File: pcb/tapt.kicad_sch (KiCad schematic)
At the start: 22 parts, among them SW1 SW_SPDT_XKB_DMx-xxxx-1, U1 nRF52810-QCxx, Y1 32MHz

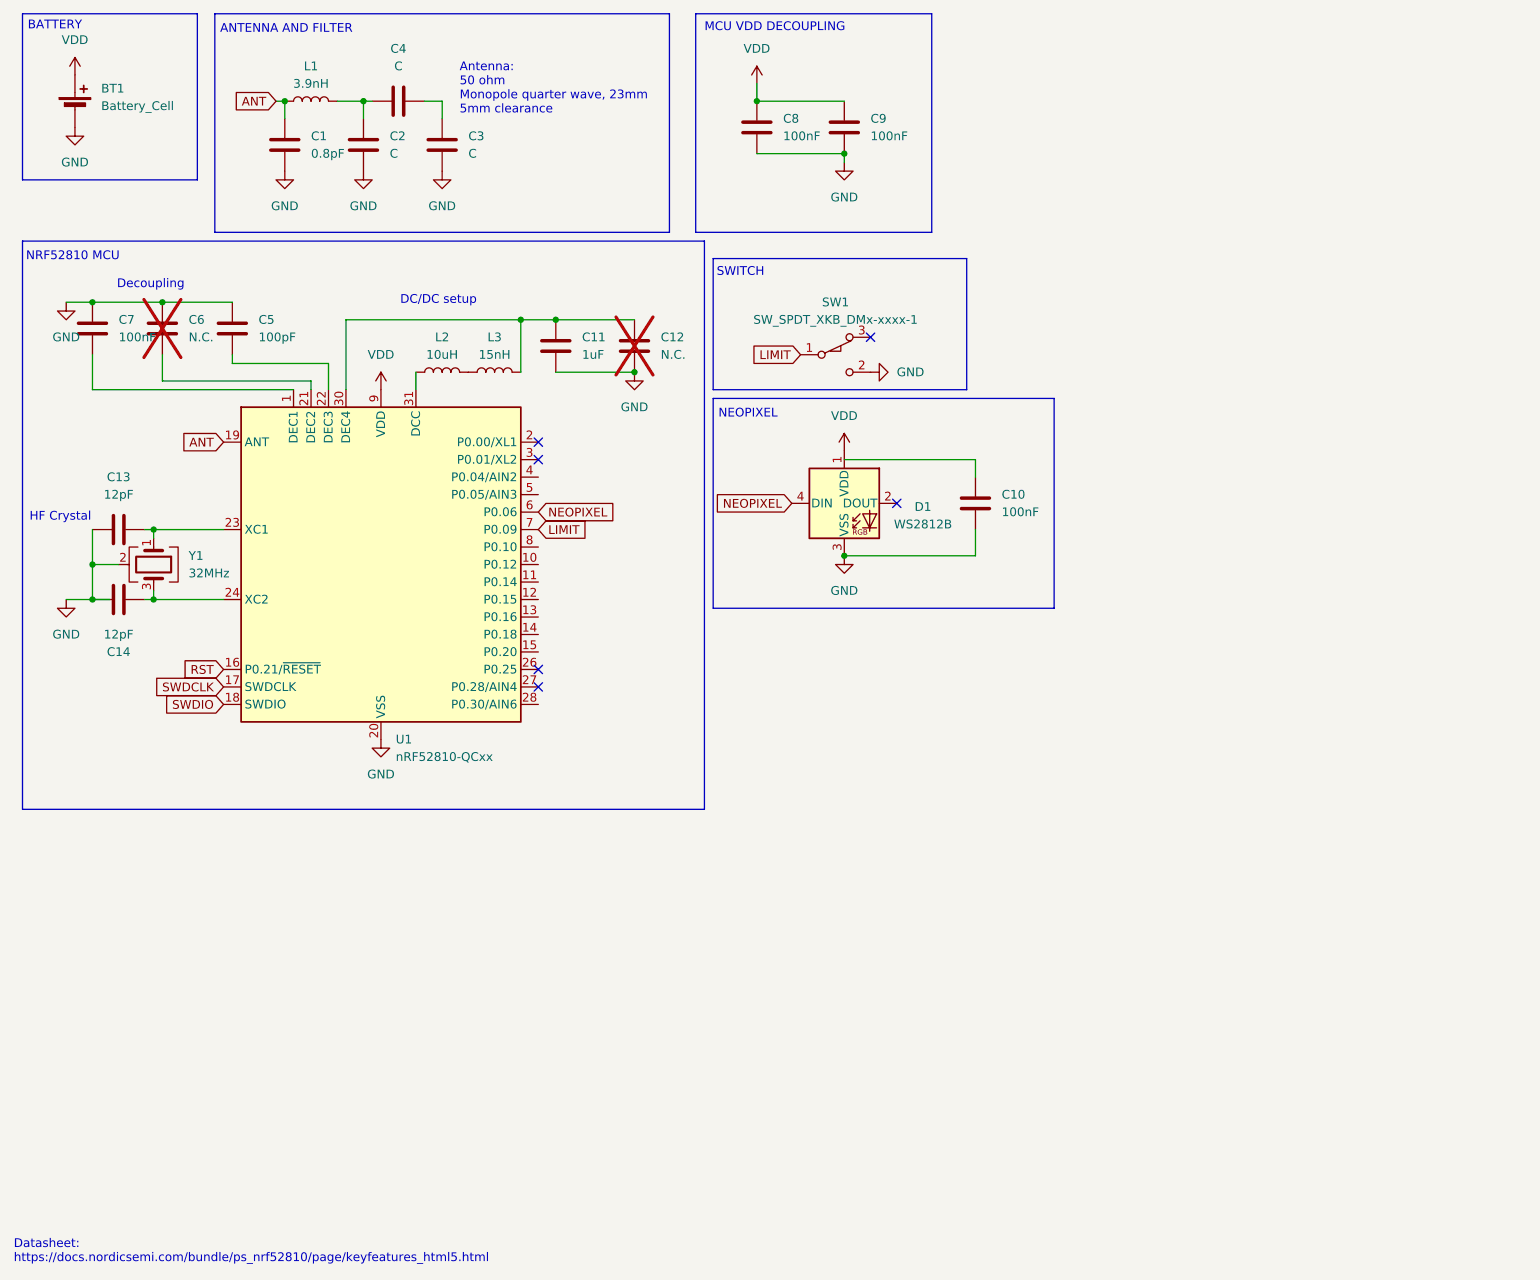
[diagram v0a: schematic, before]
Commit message: schematic: antenna, reset button
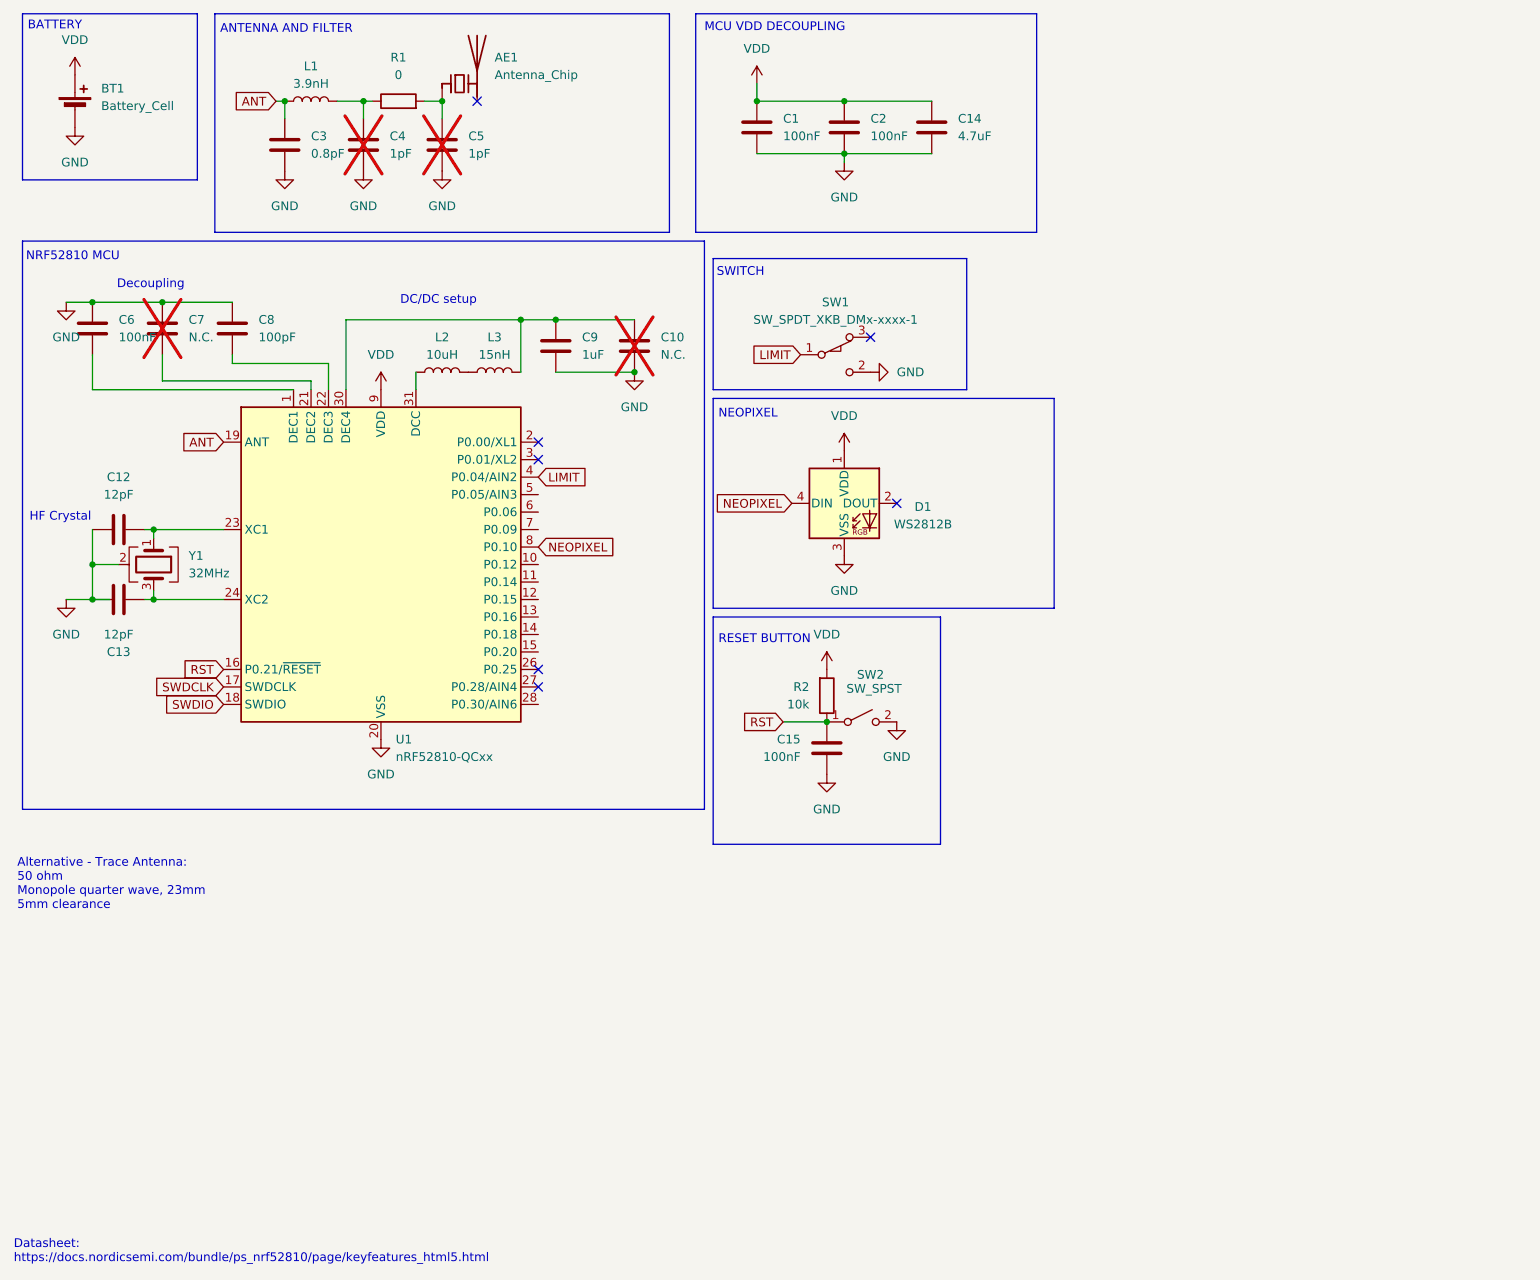
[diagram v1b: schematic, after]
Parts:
- removed C10: 100nF, Capacitor_SMD:C_0402_1005Metric, symbol Device:C
- removed C3, C4: C, symbol Device:C
- added AE1: Antenna_Chip, Inductor_SMD:L_1206_3216Metric, symbol Device:Antenna_Chip
- added C14: 4.7uF, Capacitor_SMD:C_0603_1608Metric, symbol Device:C
- added C15: 100nF, Capacitor_SMD:C_0402_1005Metric, symbol Device:C
- added C5: 1pF, Capacitor_SMD:C_0402_1005Metric, symbol Device:C
- added R1: 0, Resistor_SMD:R_0402_1005Metric, symbol Device:R
- added R2: 10k, Resistor_SMD:R_0402_1005Metric, symbol Device:R
- added SW2: SW_SPST, Button_Switch_SMD:SW_SPST_TS-1088-xR020, symbol Switch:SW_SPST
- C4: renamed from C2; value C -> 1pF; footprint (none) -> Capacitor_SMD:C_0402_1005Metric; now not fitted
- L3: footprint (none) -> Inductor_SMD:L_0402_1005Metric; LCSC (none) -> C27143
- renumbered C8 to C1, C12 to C10, C13 to C12, C14 to C13, C9 to C2, C1 to C3, C7 to C6, C6 to C7, C5 to C8, C11 to C9
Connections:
- net GND: now also C14.2, C15.2, C5.2, SW2.2 (B)
- net LIMIT: now also U1.4 (P0.04/AIN2); no longer U1.7 (P0.09)
- net NEOPIXEL: now also U1.8 (P0.10); no longer U1.6 (P0.06)
- net RST: now also C15.1, R2.1, SW2.1 (A)
- net VDD: now also C14.1, R2.2
- net at C4.1, L1.2: now also R1.1
- new net: AE1.1 (FEED), C5.1, R1.2
- no-connect marks 6 -> 7
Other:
- note added: "Alternative - Trace Antenna: 50 ohm Monopole quarter wave, 23mm 5mm clearance"
- note added: "RESET BUTTON"
- note removed: "Antenna: 50 ohm Monopole quarter wave, 23mm 5mm clearance"

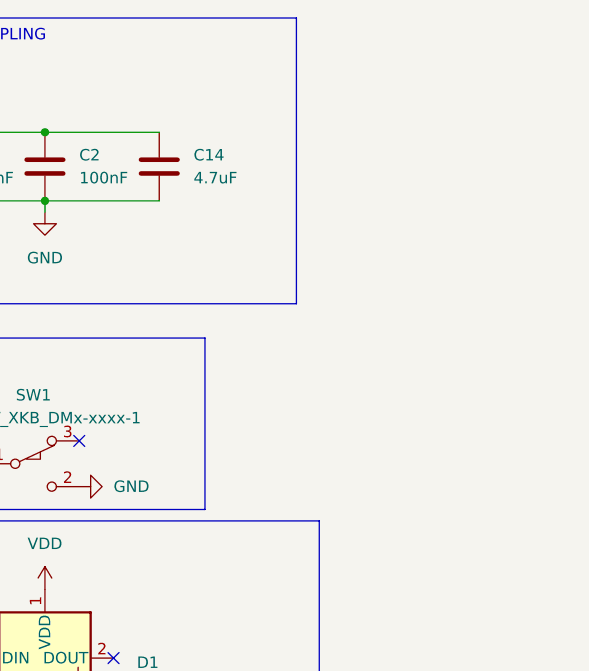
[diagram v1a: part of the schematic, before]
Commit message: major rf improvements, battery connector, component relayout
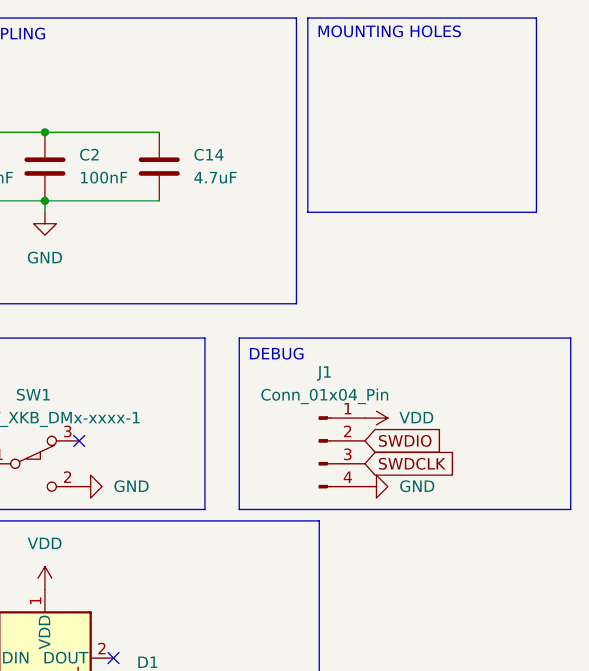
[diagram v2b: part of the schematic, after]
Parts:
- added J1: Conn_01x04_Pin, Connector_PinHeader_2.54mm:PinHeader_1x04_P2.54mm_Vertical, symbol Connector:Conn_01x04_Pin
- BT1: footprint Battery:BatteryHolder_MYOUNG_BS-07-A1BJ001_CR2032 -> Connector_Wire:SolderWire-0.5sqmm_1x02_P4.6mm_D0.9mm_OD2.1mm
- L2: footprint Capacitor_SMD:C_0603_1608Metric -> Inductor_SMD:L_0603_1608Metric
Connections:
- net GND: now also J1.4 (Pin_4)
- net SWDCLK: now also J1.3 (Pin_3)
- net SWDIO: now also J1.2 (Pin_2)
- net VDD: now also J1.1 (Pin_1)
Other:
- note added: "DEBUG"
- note added: "MOUNTING HOLES"
- company: (none) -> Siddhant Kameswar: @grimsteel
- title: (none) -> tapt

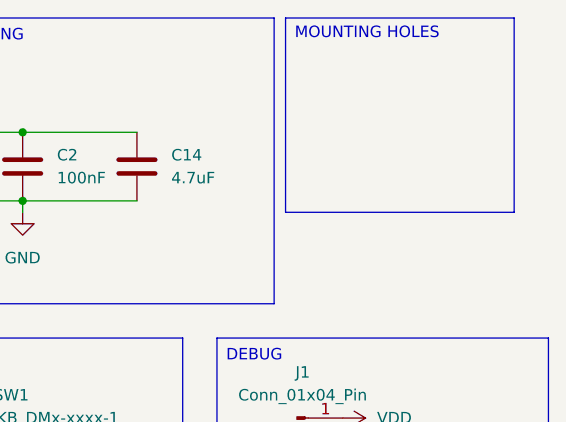
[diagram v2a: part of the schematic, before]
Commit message: add mounting holes on dogboned corners
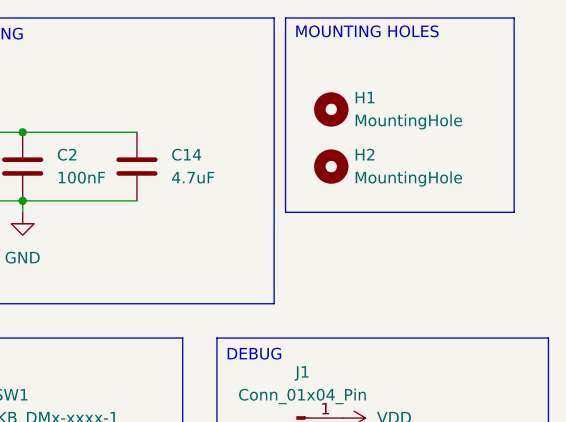
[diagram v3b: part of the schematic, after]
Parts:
- added H1, H2: MountingHole, MountingHole:MountingHole_2.7mm_M2.5, symbol Mechanical:MountingHole
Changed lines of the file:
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@@
+	)
+	(symbol
+		(lib_id "Mechanical:MountingHole")
+		(at 168.91 24.13 0)
+		(unit 1)
+		(exclude_from_sim no)
+		(in_bom no)
+		(on_board yes)
+		(dnp no)
+		(fields_autoplaced yes)
+		(property "Reference" "H1"
+			(at 171.45 22.8599 0)
+			(effects
+				(font
+					(size 1.27 1.27)
+				)
+				(justify left)
+			)
+		)
+		(property "Value" "MountingHole"
+			(at 171.45 25.3999 0)
+			(effects
+				(font
+					(size 1.27 1.27)
+				)
+				(justify left)
+			)
+		)
+		(property "Footprint" "MountingHole:MountingHole_2.7mm_M2.5"
+			(at 168.91 24.13 0)
+			(effects
+				(font
+					(size 1.27 1.27)
+				)
+				(hide yes)
+			)
+		)
+		(property "Datasheet" "~"
+			(at 168.91 24.13 0)
+			(effects
+				(font
+					(size 1.27 1.27)
+				)
+				(hide yes)
+			)
+		)
+		(property "Description" "Mounting Hole without connection"
+			(at 168.91 24.13 0)
+			(effects
+				(font
+					(size 1.27 1.27)
+				)
+				(hide yes)
+			)
+		)
+		(instances
+			(project ""
+				(path "/5229fa67-90ff-468b-81bc-87113a360bb5"
+					(reference "H1")
+					(unit 1)
+				)
+			)
+		)
 	)
 	(symbol
@@
 					(unit 1)
 				)
+			)
+		)
+	)
+	(symbol
+		(lib_id "Mechanical:MountingHole")
+		(at 168.91 30.48 0)
+		(unit 1)
+		(exclude_from_sim no)
+		(in_bom no)
+		(on_board yes)
+		(dnp no)
+		(fields_autoplaced yes)
+		(property "Reference" "H2"
+			(at 171.45 29.2099 0)
+			(effects
+				(font
+					(size 1.27 1.27)
+				)
+				(justify left)
+			)
+		)
+		(property "Value" "MountingHole"
+			(at 171.45 31.7499 0)
+			(effects
+				(font
+					(size 1.27 1.27)
+				)
+				(justify left)
+			)
+		)
+		(property "Footprint" "MountingHole:MountingHole_2.7mm_M2.5"
+			(at 168.91 30.48 0)
+			(effects
+				(font
+					(size 1.27 1.27)
+				)
+				(hide yes)
+			)
+		)
+		(property "Datasheet" "~"
+			(at 168.91 30.48 0)
+			(effects
+				(font
+					(size 1.27 1.27)
+				)
+				(hide yes)
+			)
+		)
+		(property "Description" "Mounting Hole without connection"
+			(at 168.91 30.48 0)
+			(effects
+				(font
+					(size 1.27 1.27)
+				)
+				(hide yes)
+			)
+		)
+		(instances
+			(project "tapt"
+				(path "/5229fa67-90ff-468b-81bc-87113a360bb5"
+					(reference "H2")
+					(unit 1)
+				)

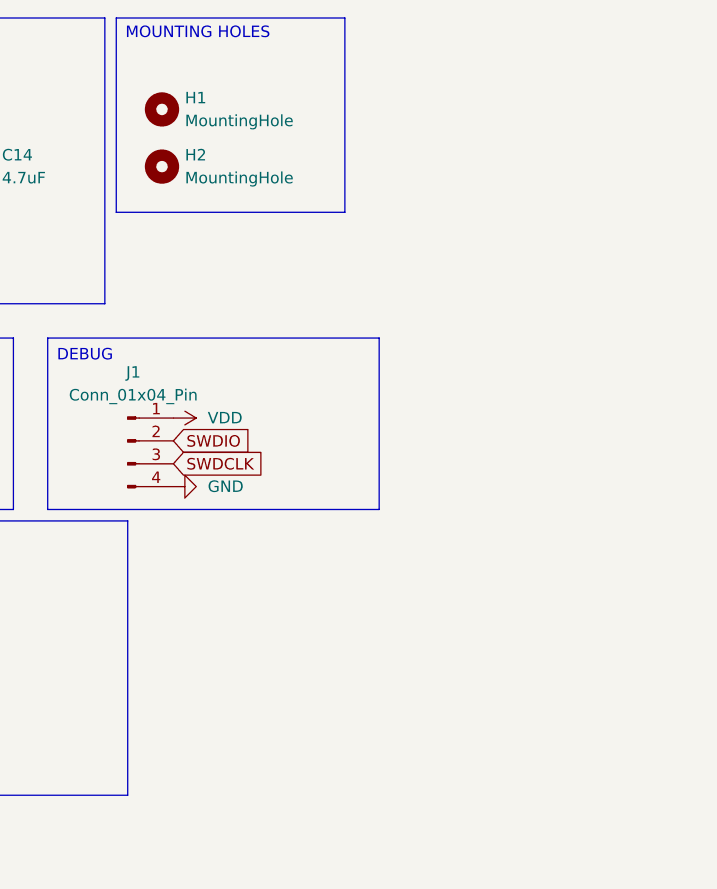
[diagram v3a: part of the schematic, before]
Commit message: schematic: status led, uart
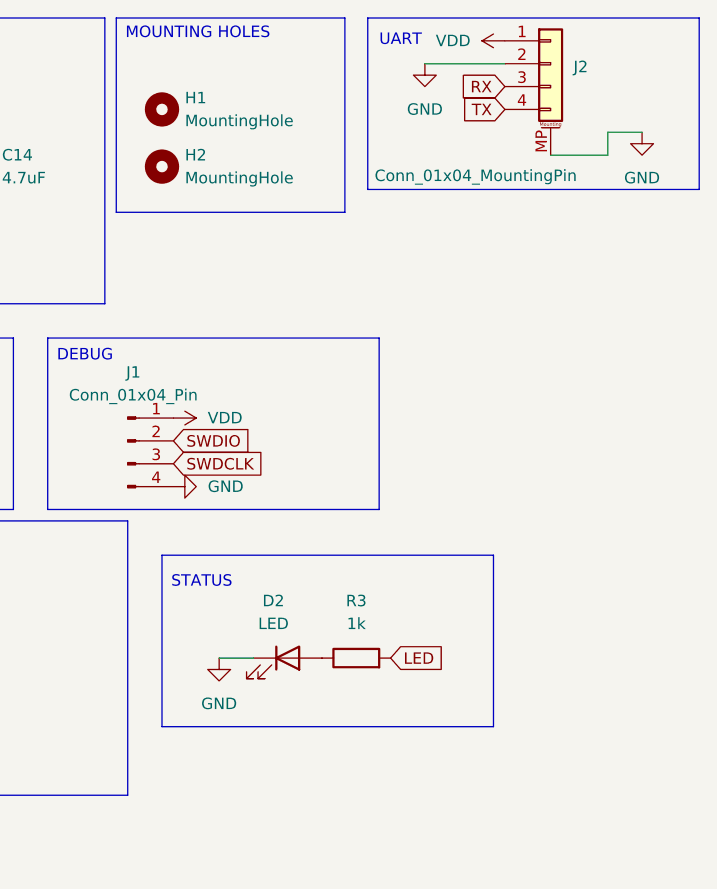
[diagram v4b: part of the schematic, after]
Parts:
- added D2: LED, LED_SMD:LED_0805_2012Metric, symbol Device:LED
- added J2: Conn_01x04_MountingPin, Connector_JST:JST_SH_BM04B-SRSS-TB_1x04-1MP_P1.00mm_Vertical, symbol Connector_Generic_MountingPin:Conn_01x04_MountingPin
- added R3: 1k, Resistor_SMD:R_0805_2012Metric, symbol Device:R
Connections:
- net GND: now also D2.1 (K), J2.2 (Pin_2), J2.MP (MountPin)
- net VDD: now also J2.1 (Pin_1)
- new net: D2.2 (A), R3.1
- new net LED: R3.2
- new net RX: J2.3 (Pin_3)
- new net TX: J2.4 (Pin_4)
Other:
- note added: "STATUS"
- note added: "UART"
